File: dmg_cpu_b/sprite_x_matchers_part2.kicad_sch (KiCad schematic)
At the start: 90 parts

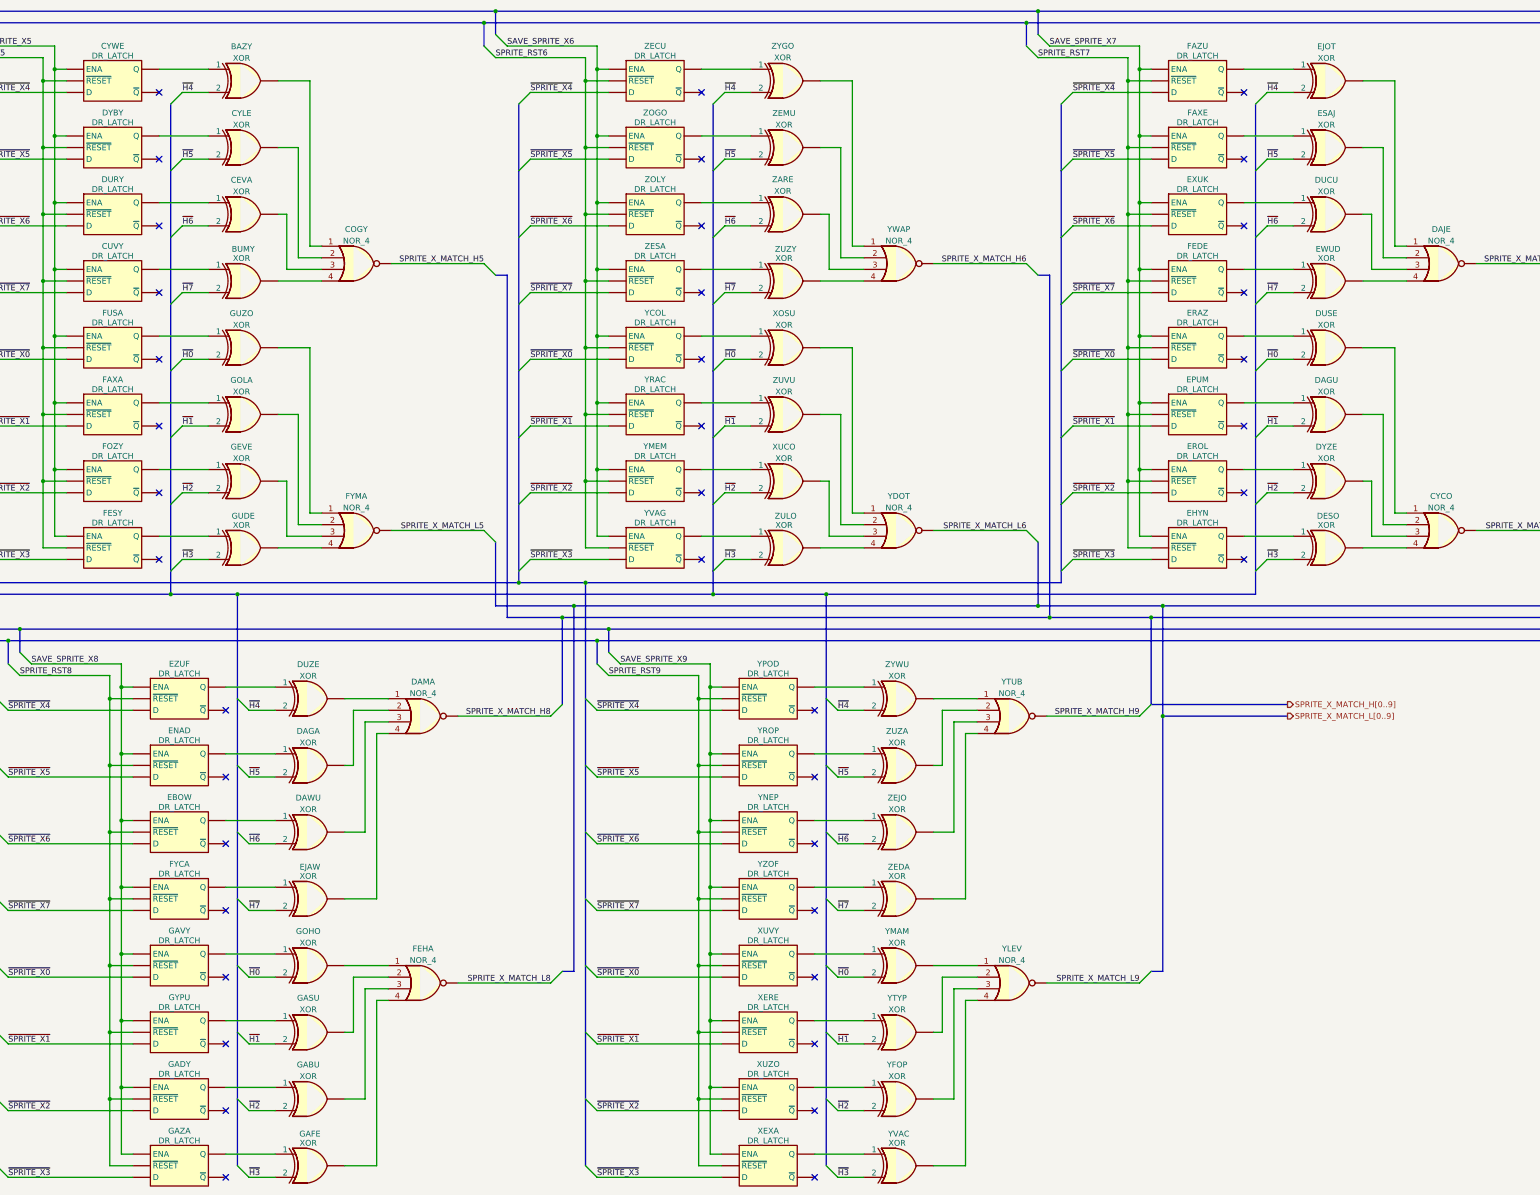
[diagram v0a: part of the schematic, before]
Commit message: Give more meaningful names to cell types
Before this commit, many of the cells types in the chip were named in a
sloppy manner. The different inverter, latch and flip flop valiants were
just suffixed with A, B, C, D, ... Those suffixes gave no information
about the actual differences. They had to be looked up in the
documentation. Now the names of cell types with different variants have
changed:

* Inverter types are named NOT_X1, NOT_X2, NOT_X3, ... The _Xn suffix
  reflects the drive strength of the cell. X1 is the drive strength of
  the weakest inverter, X2 is double the drive strength of the weakest
  inverter.
* Flip flop types are named DFFR, DFFR_CC, DFFR_CC_Q. DFFR is a normal
  data flip flop with reset and a single clock input. The suffix _CC is
  added to flip flops that have two complementary clock inputs (CLK and
  /CLK). Flip flops that only have the positive Q output are suffixed
  with _Q.
* Latch types are named similar to flip flops: DLATCH, DLATCH_EE,
  DLATCH_EE_Q. The suffix _EE is given to latches that require
  "externally inverted enable" signals (ENA and /ENA).
* I/O pad types all start with PAD_BIDIR, PAD_IN or PAD_OUT. They also
  have suffixes that describe what makes them unique, like _PU for
  pull-ups.

Other minor changes were made to align the names with common naming
schemes of other cell libraries.
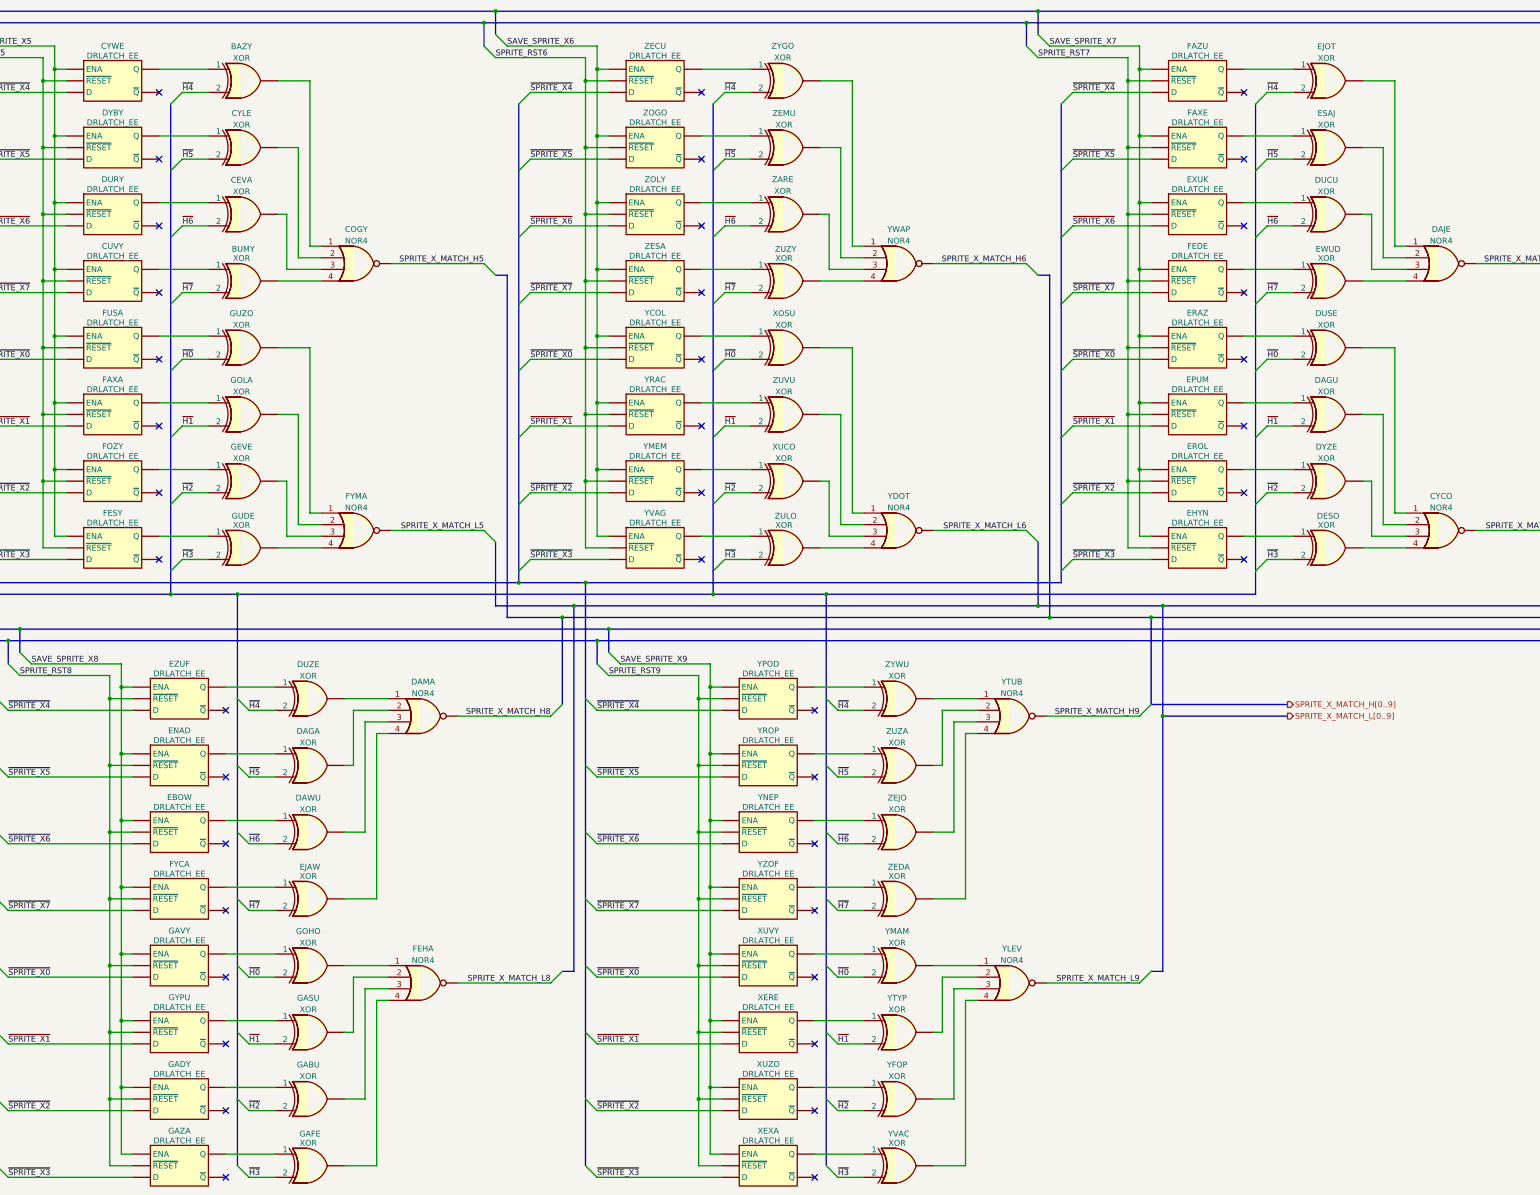
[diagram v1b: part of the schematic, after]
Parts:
- COGY, CYCO, DAJE, DAMA, FEHA, FYMA, YDOT, YLEV, YTUB, YWAP: value NOR_4 -> NOR4; symbol DMG_CPU_Cells:NOR_4 -> DMG_CPU_Cells:NOR4
- CUVY, CYWE, DURY, DYBY, EBOW, EHYN, ENAD, EPUM, ERAZ, EROL, EXUK, EZUF, FAXA, FAXE, FAZU, FEDE, FESY, FOZY, FUSA, FYCA, GADY, GAVY, GAZA, GYPU, XERE, XEXA, XUVY, XUZO, YCOL, YMEM, YNEP, YPOD, YRAC, YROP, YVAG, YZOF, ZECU, ZESA, ZOGO, ZOLY: value DR_LATCH -> DRLATCH_EE; symbol DMG_CPU_Cells:DR_LATCH -> DMG_CPU_Cells:DRLATCH_EE

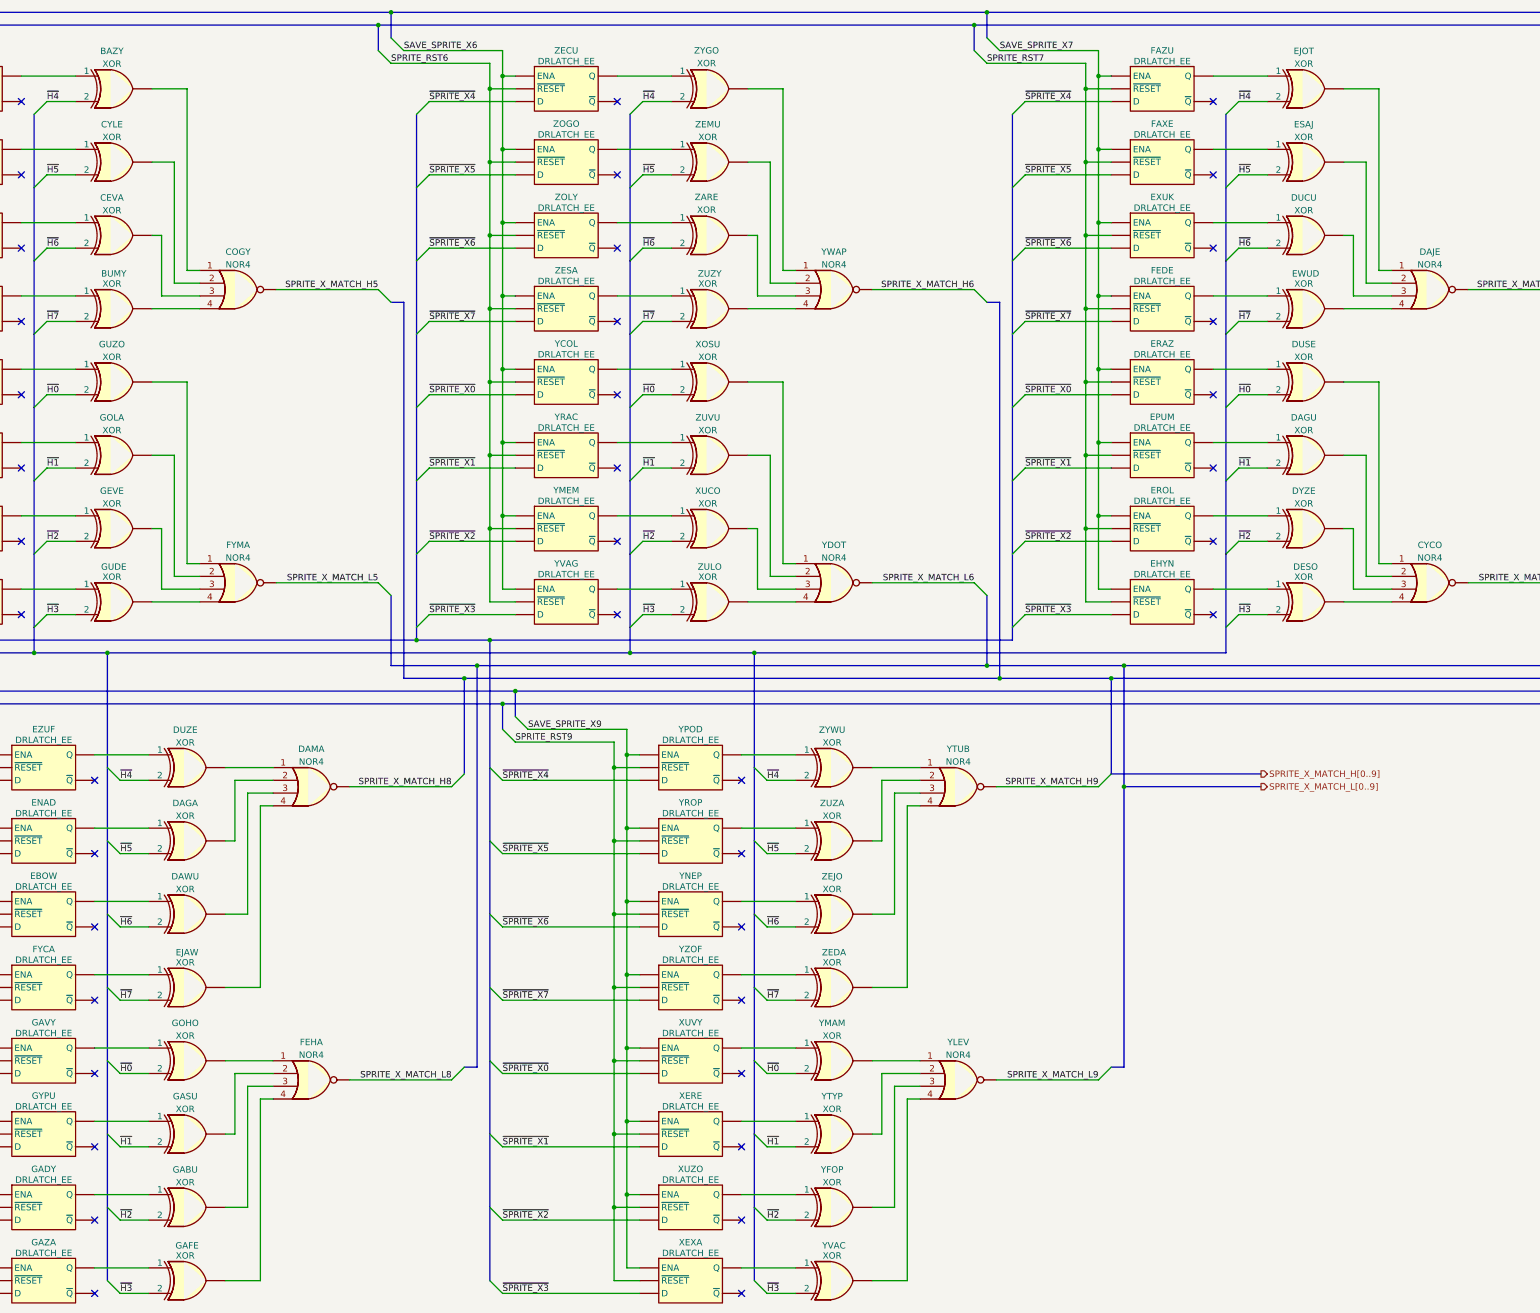
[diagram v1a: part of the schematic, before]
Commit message: SM83 Layout: Add bottom part of sequencer cells
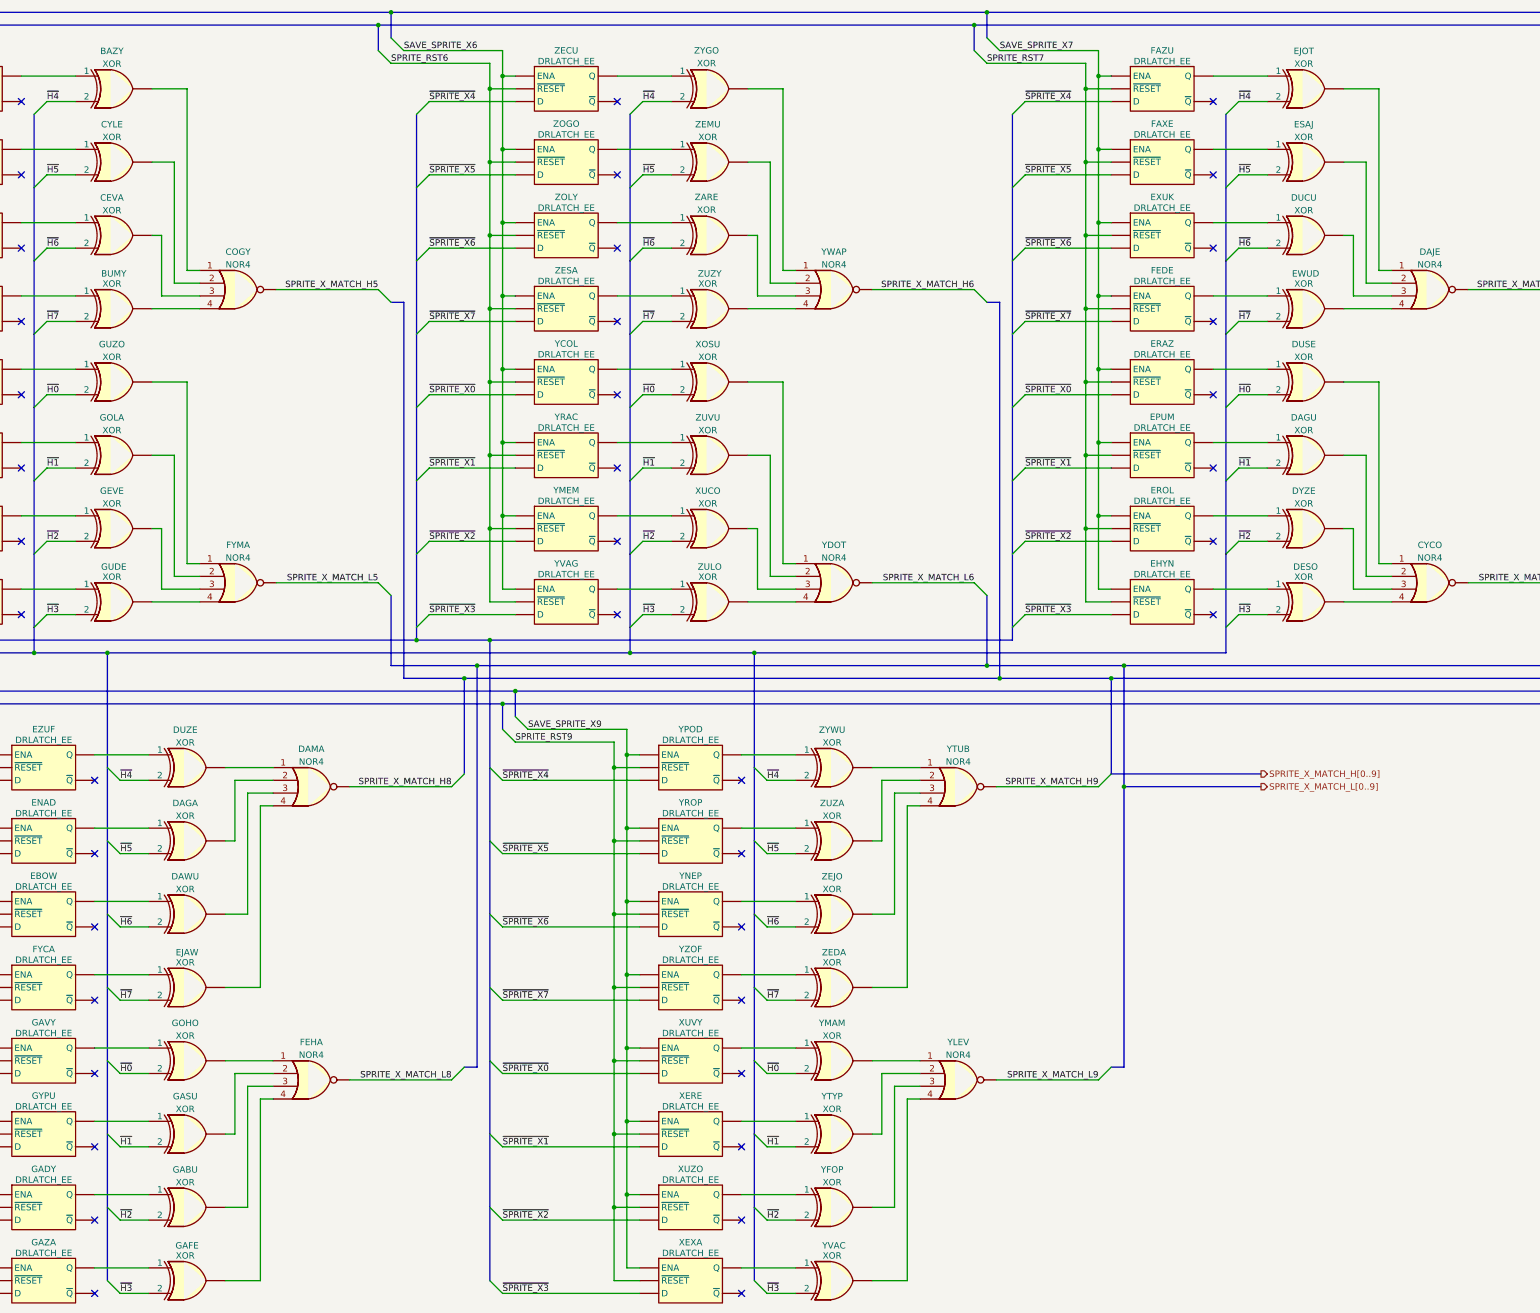
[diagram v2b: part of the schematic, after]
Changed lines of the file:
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@@
 (kicad_sch
-	(version 20231120)
+	(version 20250114)
 	(generator "eeschema")
-	(generator_version "8.0")
+	(generator_version "9.0")
 	(paper "A3")
 	(title_block
 		(title "DMG-CPU B")
-		(date "2025-04-12")
+		(date "2025-04-22")
 		(rev "0.7")
 		(company "CC-BY-SA-4.0 Régis Galland & Michael Singer -- Derived work from Furrtek")
